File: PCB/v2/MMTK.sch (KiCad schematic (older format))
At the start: 9 parts, among them J2 Stepper

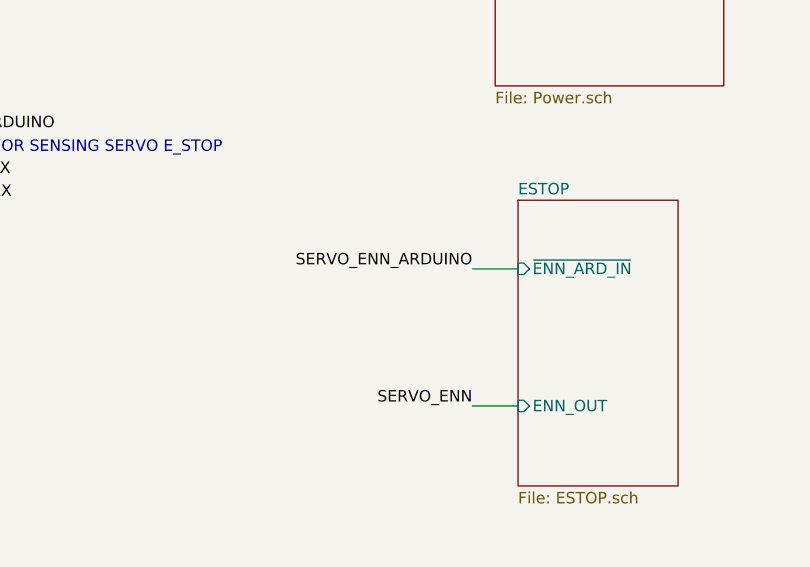
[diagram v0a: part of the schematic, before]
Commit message: Add 12V to ENN Loop
Added 12v detection to ENN loop, so EN on tmc would be high if 12v not present but 5v is.
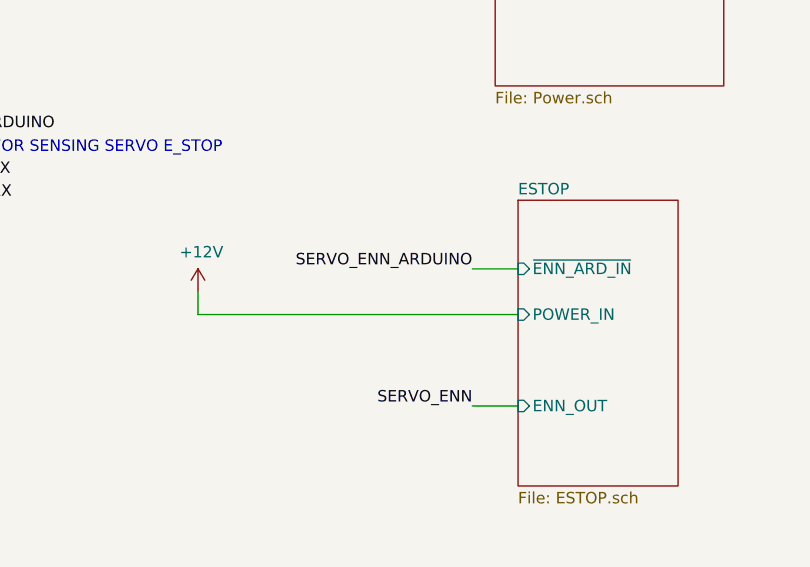
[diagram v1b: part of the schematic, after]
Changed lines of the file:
@@
 F2 "ENN_OUT" I L 9600 3400 50
 F3 "~ENN_ARD_IN" I L 9600 2800 50
+F4 "POWER_IN" I L 9600 3000 50
 $EndSheet
 Wire Wire Line
@@
 NoConn ~ 4000 1600
 NoConn ~ 4000 1700
+$Comp
+L MMTK-rescue:+12V-power-MMTK-rescue-MMTK-rescue #PWR?
+U 1 1 628C8A16
+P 8200 2900
+F 0 "#PWR?" H 8200 2750 50  0001 C CNN
+F 1 "+12V" H 8215 3073 50  0000 C CNN
+F 2 "" H 8200 2900 50  0001 C CNN
+F 3 "" H 8200 2900 50  0001 C CNN
+	1    8200 2900
+	1    0    0    -1
+$EndComp
+Wire Wire Line
+	8200 2900 8200 3000
+Wire Wire Line
+	8200 3000 9600 3000
 $EndSCHEMATC
